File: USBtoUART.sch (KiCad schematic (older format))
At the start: 17 parts

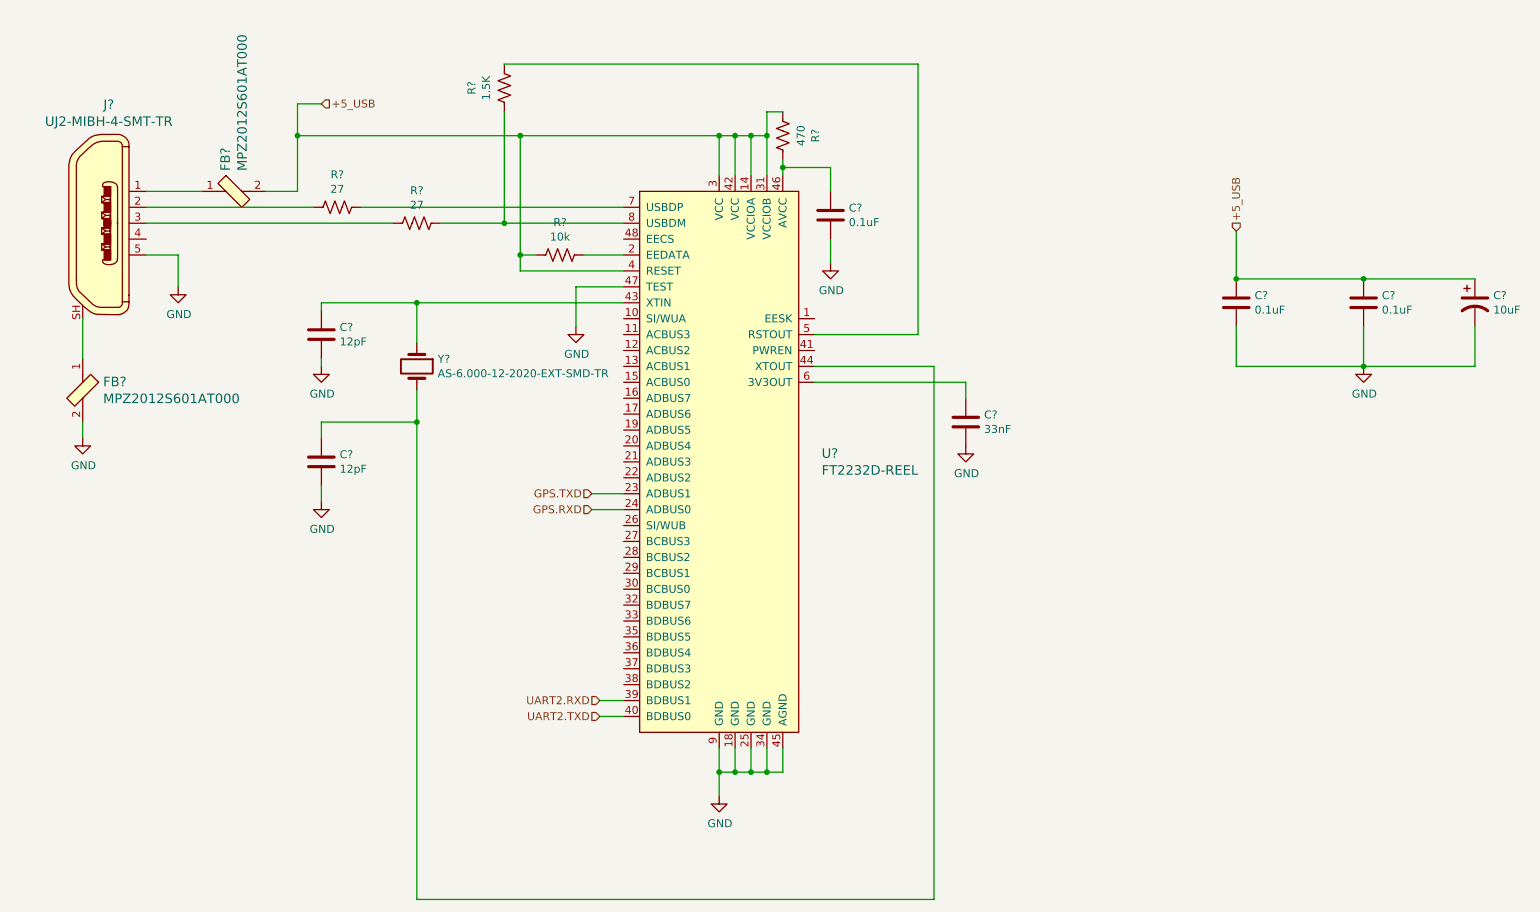
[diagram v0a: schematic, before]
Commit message: Annotated schematics and added UART Jumpers
Annotated schematics.

Added jumpers to GPS UART because I'm still not 100% sure on the connections and I don't want to have to respin a board because I was wrong.
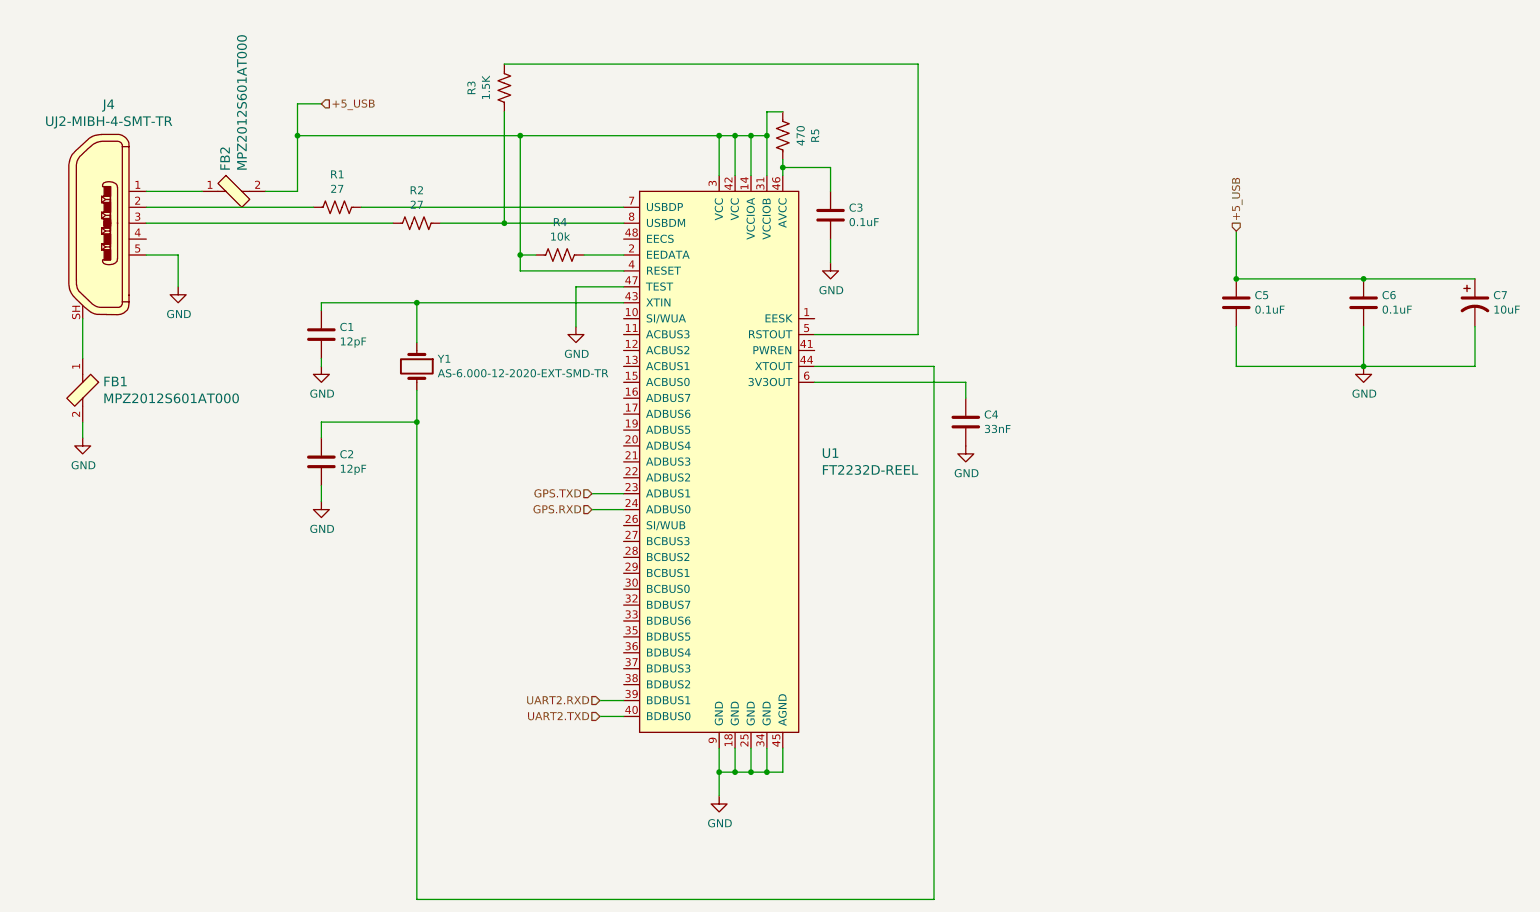
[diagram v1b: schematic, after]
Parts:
- gave numbers to parts that had none: 17
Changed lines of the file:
@@
 $EndDescr
 $Comp
-L dk_Interface-Controllers:FT2232D-REEL U?
+L dk_Interface-Controllers:FT2232D-REEL U1
 U 1 1 5F8465F0
 P 5450 2500
-F 0 "U?" H 5894 1453 60  0000 L CNN
+F 0 "U1" H 5894 1453 60  0000 L CNN
 F 1 "FT2232D-REEL" H 5894 1347 60  0000 L CNN
 F 2 "digikey-footprints:LQFP-48_7x7mm" V 5650 2700 60  0001 L CNN
@@
 $EndComp
 $Comp
-L dk_USB-DVI-HDMI-Connectors:UJ2-MIBH-4-SMT-TR J?
+L dk_USB-DVI-HDMI-Connectors:UJ2-MIBH-4-SMT-TR J4
 U 1 1 5F847751
 P 1350 2100
-F 0 "J?" H 1414 2845 60  0000 C CNN
+F 0 "J4" H 1414 2845 60  0000 C CNN
 F 1 "UJ2-MIBH-4-SMT-TR" H 1414 2739 60  0000 C CNN
 F 2 "digikey-footprints:USB_Micro_B_Male_UJ2-MIBH-4-SMT-TR" H 1550 2300 60  0001 L CNN
@@
 $EndComp
 $Comp
-L power:GND #PWR?
+L power:GND #PWR03
 U 1 1 5F848CF8
 P 1850 2500
-F 0 "#PWR?" H 1850 2250 50  0001 C CNN
+F 0 "#PWR03" H 1850 2250 50  0001 C CNN
 F 1 "GND" H 1855 2327 50  0000 C CNN
 F 2 "" H 1850 2500 50  0001 C CNN
@@
 $EndComp
 $Comp
-L dk_Ferrite-Beads-and-Chips:MPZ2012S601AT000 FB?
+L dk_Ferrite-Beads-and-Chips:MPZ2012S601AT000 FB1
 U 1 1 5F84934E
 P 1250 3150
-F 0 "FB?" V 1197 3278 60  0000 L CNN
+F 0 "FB1" V 1197 3278 60  0000 L CNN
 F 1 "MPZ2012S601AT000" V 1303 3278 60  0000 L CNN
 F 2 "digikey-footprints:0805" H 1450 3350 60  0001 L CNN
@@
 	1250 2700 1250 2950
 $Comp
-L power:GND #PWR?
+L power:GND #PWR02
 U 1 1 5F84BCF3
 P 1250 3450
-F 0 "#PWR?" H 1250 3200 50  0001 C CNN
+F 0 "#PWR02" H 1250 3200 50  0001 C CNN
 F 1 "GND" H 1255 3277 50  0000 C CNN
 F 2 "" H 1250 3450 50  0001 C CNN
@@
 	1250 3350 1250 3450
 $Comp
-L dk_Ferrite-Beads-and-Chips:MPZ2012S601AT000 FB?
+L dk_Ferrite-Beads-and-Chips:MPZ2012S601AT000 FB2
 U 1 1 5F84C701
 P 2200 1900
-F 0 "FB?" V 2147 2028 60  0000 L CNN
+F 0 "FB2" V 2147 2028 60  0000 L CNN
 F 1 "MPZ2012S601AT000" V 2253 2028 60  0000 L CNN
 F 2 "digikey-footprints:0805" H 2400 2100 60  0001 L CNN
@@
 	1650 1900 2000 1900
 $Comp
-L Device:C C?
+L Device:C C4
 U 1 1 5F84E28B
 P 6800 3350
-F 0 "C?" H 6915 3396 50  0000 L CNN
+F 0 "C4" H 6915 3396 50  0000 L CNN
 F 1 "33nF" H 6915 3305 50  0000 L CNN
 F 2 "Capacitor_SMD:C_0805_2012Metric_Pad1.18x1.45mm_HandSolder" H 6800 3350 50  0001 C CNN
@@
 	6800 3100 6800 3200
 $Comp
-L Device:C C?
+L Device:C C5
 U 1 1 5F84FF63
 P 8500 2600
-F 0 "C?" H 8615 2646 50  0000 L CNN
+F 0 "C5" H 8615 2646 50  0000 L CNN
 F 1 "0.1uF" H 8615 2555 50  0000 L CNN
 F 2 "Capacitor_SMD:C_0805_2012Metric_Pad1.18x1.45mm_HandSolder" H 8500 2600 50  0001 C CNN
@@
 $EndComp
 $Comp
-L Device:C C?
+L Device:C C6
 U 1 1 5F850987
 P 9300 2600
-F 0 "C?" H 9415 2646 50  0000 L CNN
+F 0 "C6" H 9415 2646 50  0000 L CNN
 F 1 "0.1uF" H 9415 2555 50  0000 L CNN
 F 2 "Capacitor_SMD:C_0805_2012Metric_Pad1.18x1.45mm_HandSolder" H 9300 2600 50  0001 C CNN
@@
 $EndComp
 $Comp
-L Device:CP1 C?
+L Device:CP1 C7
 U 1 1 5F853226
 P 10000 2600
-F 0 "C?" H 10115 2646 50  0000 L CNN
+F 0 "C7" H 10115 2646 50  0000 L CNN
 F 1 "10uF" H 10115 2555 50  0000 L CNN
 F 2 "Capacitor_Tantalum_SMD:CP_EIA-3216-10_Kemet-I_Pad1.58x1.35mm_HandSolder" H 10000 2600 50  0001 C CNN
@@
 $EndComp
 $Comp
-L Device:R_US R?
+L Device:R_US R1
 U 1 1 5F85B62B
 P 2850 2000
-F 0 "R?" V 2645 2000 50  0000 C CNN
+F 0 "R1" V 2645 2000 50  0000 C CNN
 F 1 "27" V 2736 2000 50  0000 C CNN
 F 2 "Resistor_SMD:R_0805_2012Metric_Pad1.20x1.40mm_HandSolder" V 2890 1990 50  0001 C CNN
@@
 $EndComp
 $Comp
-L Device:R_US R?
+L Device:R_US R2
 U 1 1 5F85C9ED
 P 3350 2100
-F 0 "R?" V 3145 2100 50  0000 C CNN
+F 0 "R2" V 3145 2100 50  0000 C CNN
 F 1 "27" V 3236 2100 50  0000 C CNN
 F 2 "Resistor_SMD:R_0805_2012Metric_Pad1.20x1.40mm_HandSolder" V 3390 2090 50  0001 C CNN
@@
 	1650 2100 3200 2100
 $Comp
-L Device:R_US R?
+L Device:R_US R3
 U 1 1 5F85D849
 P 3900 1250
-F 0 "R?" V 3695 1250 50  0000 C CNN
+F 0 "R3" V 3695 1250 50  0000 C CNN
 F 1 "1.5K" V 3786 1250 50  0000 C CNN
 F 2 "Resistor_SMD:R_0805_2012Metric_Pad1.20x1.40mm_HandSolder" V 3940 1240 50  0001 C CNN
@@
 	4500 5100 4650 5100
 $Comp
-L Device:Crystal Y?
+L Device:Crystal Y1
 U 1 1 5F86847C
 P 3350 3000
-F 0 "Y?" V 3304 3131 50  0000 L CNN
+F 0 "Y1" V 3304 3131 50  0000 L CNN
 F 1 "AS-6.000-12-2020-EXT-SMD-TR" V 3395 3131 50  0000 L CNN
 F 2 "Crystal:Crystal_SMD_HC49-SD_HandSoldering" H 3350 3000 50  0001 C CNN
@@
 	6600 3000 5850 3000
 $Comp
-L Device:C C?
+L Device:C C1
 U 1 1 5F869A1D
 P 2750 2800
-F 0 "C?" H 2865 2846 50  0000 L CNN
+F 0 "C1" H 2865 2846 50  0000 L CNN
 F 1 "12pF" H 2865 2755 50  0000 L CNN
 F 2 "Capacitor_SMD:C_0805_2012Metric_Pad1.18x1.45mm_HandSolder" H 2750 2800 50  0001 C CNN
@@
 $EndComp
 $Comp
-L Device:C C?
+L Device:C C2
 U 1 1 5F86A608
 P 2750 3600
-F 0 "C?" H 2865 3646 50  0000 L CNN
+F 0 "C2" H 2865 3646 50  0000 L CNN
 F 1 "12pF" H 2865 3555 50  0000 L CNN
 F 2 "Capacitor_SMD:C_0805_2012Metric_Pad1.18x1.45mm_HandSolder" H 2750 3600 50  0001 C CNN
@@
 $EndComp
 $Comp
-L power:GND #PWR?
+L power:GND #PWR04
 U 1 1 5F86A976
 P 2750 3000
-F 0 "#PWR?" H 2750 2750 50  0001 C CNN
+F 0 "#PWR04" H 2750 2750 50  0001 C CNN
 F 1 "GND" H 2755 2827 50  0000 C CNN
 F 2 "" H 2750 3000 50  0001 C CNN
@@
 $EndComp
 $Comp
-L power:GND #PWR?
+L power:GND #PWR05
 U 1 1 5F86AC39
 P 2750 3850
-F 0 "#PWR?" H 2750 3600 50  0001 C CNN
+F 0 "#PWR05" H 2750 3600 50  0001 C CNN
 F 1 "GND" H 2755 3677 50  0000 C CNN
 F 2 "" H 2750 3850 50  0001 C CNN
@@
 	2750 2950 2750 3000
 $Comp
-L power:GND #PWR?
+L power:GND #PWR010
 U 1 1 5F88F94A
 P 9300 3000
-F 0 "#PWR?" H 9300 2750 50  0001 C CNN
+F 0 "#PWR010" H 9300 2750 50  0001 C CNN
 F 1 "GND" H 9305 2827 50  0000 C CNN
 F 2 "" H 9300 3000 50  0001 C CNN
@@
 	5250 1550 5350 1550
 $Comp
-L Device:C C?
+L Device:C C3
 U 1 1 5F894C10
 P 5950 2050
-F 0 "C?" H 6065 2096 50  0000 L CNN
+F 0 "C3" H 6065 2096 50  0000 L CNN
 F 1 "0.1uF" H 6065 2005 50  0000 L CNN
 F 2 "Capacitor_SMD:C_0805_2012Metric_Pad1.18x1.45mm_HandSolder" H 5950 2050 50  0001 C CNN
@@
 $EndComp
 $Comp
-L Device:R_US R?
+L Device:R_US R5
 U 1 1 5F895D20
 P 5650 1550
-F 0 "R?" V 5445 1550 50  0000 C CNN
+F 0 "R5" V 5445 1550 50  0000 C CNN
 F 1 "470" V 5536 1550 50  0000 C CNN
 F 2 "Resistor_SMD:R_0805_2012Metric_Pad1.20x1.40mm_HandSolder" V 5690 1540 50  0001 C CNN
@@
 Connection ~ 5550 1550
 $Comp
-L power:GND #PWR?
+L power:GND #PWR08
 U 1 1 5F898B74
 P 5950 2350
-F 0 "#PWR?" H 5950 2100 50  0001 C CNN
+F 0 "#PWR08" H 5950 2100 50  0001 C CNN
 F 1 "GND" H 5955 2177 50  0000 C CNN
 F 2 "" H 5950 2350 50  0001 C CNN
@@
 	5950 2350 5950 2200
 $Comp
-L power:GND #PWR?
+L power:GND #PWR09
 U 1 1 5F899BAF
 P 6800 3500
-F 0 "#PWR?" H 6800 3250 50  0001 C CNN
+F 0 "#PWR09" H 6800 3250 50  0001 C CNN
 F 1 "GND" H 6805 3327 50  0000 C CNN
 F 2 "" H 6800 3500 50  0001 C CNN
@@
 Connection ~ 9300 2450
 $Comp
-L power:GND #PWR?
+L power:GND #PWR07
 U 1 1 5F89EA9A
 P 5250 5700
-F 0 "#PWR?" H 5250 5450 50  0001 C CNN
+F 0 "#PWR07" H 5250 5450 50  0001 C CNN
 F 1 "GND" H 5255 5527 50  0000 C CNN
 F 2 "" H 5250 5700 50  0001 C CNN
@@
 	5550 5550 5450 5550
 $Comp
-L power:GND #PWR?
+L power:GND #PWR06
 U 1 1 5F8A43C4
 P 4350 2750
-F 0 "#PWR?" H 4350 2500 50  0001 C CNN
+F 0 "#PWR06" H 4350 2500 50  0001 C CNN
 F 1 "GND" H 4355 2577 50  0000 C CNN
 F 2 "" H 4350 2750 50  0001 C CNN
@@
 	5850 2800 6500 2800
 $Comp
-L Device:R_US R?
+L Device:R_US R4
 U 1 1 5F8B2661
 P 4250 2300
-F 0 "R?" V 4045 2300 50  0000 C CNN
+F 0 "R4" V 4045 2300 50  0000 C CNN
 F 1 "10k" V 4136 2300 50  0000 C CNN
 F 2 "Resistor_SMD:R_0805_2012Metric_Pad1.20x1.40mm_HandSolder" V 4290 2290 50  0001 C CNN

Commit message: completed connections
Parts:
- added JP? (x2): JUMPER-SMT_3_1-NC, SMT-JUMPER_3_1-NC, symbol SparkFun-Jumpers:JUMPER-SMT_3_1-NC
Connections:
- net UART2.RXD: now also JP?.1, JP?.3; no longer U1.39 (BDBUS1)
- net UART2.TXD: now also JP?.1, JP?.3; no longer U1.40 (BDBUS0)
- new net: JP?.2, U1.39 (BDBUS1)
- new net: JP?.2, U1.40 (BDBUS0)
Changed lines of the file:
@@
 $Descr A4 11693 8268
 encoding utf-8
-Sheet 3 4
+Sheet 2 4
 Title ""
 Date ""
@@
 Wire Wire Line
 	4450 3800 4650 3800
-Text HLabel 4500 5100 0    50   Input ~ 0
+Text HLabel 1400 4800 0    50   Input ~ 0
 UART2.RXD
-Text HLabel 4500 5200 0    50   Input ~ 0
+Text HLabel 1400 5900 0    50   Input ~ 0
 UART2.TXD
-Wire Wire Line
-	4500 5200 4650 5200
-Wire Wire Line
-	4500 5100 4650 5100
 $Comp
 L Device:Crystal Y1
@@
 Wire Wire Line
 	4400 2300 4650 2300
+$Comp
+L SparkFun-Jumpers:JUMPER-SMT_3_1-NC JP?
+U 1 1 5F8D37AA
+P 2000 5000
+F 0 "JP?" H 2104 4905 45  0000 L CNN
+F 1 "JUMPER-SMT_3_1-NC" H 2104 4989 45  0000 L CNN
+F 2 "SMT-JUMPER_3_1-NC" H 2000 5250 20  0001 C CNN
+F 3 "" V 2000 4945 60  0001 C CNN
+F 4 "XXX-00000" H 2104 5084 60  0000 L CNN "PROD_ID"
+	1    2000 5000
+	-1   0    0    1
+$EndComp
+$Comp
+L SparkFun-Jumpers:JUMPER-SMT_3_1-NC JP?
+U 1 1 5F8DF40E
+P 1750 5700
+F 0 "JP?" H 1854 5605 45  0000 L CNN
+F 1 "JUMPER-SMT_3_1-NC" H 1854 5689 45  0000 L CNN
+F 2 "SMT-JUMPER_3_1-NC" H 1750 5950 20  0001 C CNN
+F 3 "" V 1750 5645 60  0001 C CNN
+F 4 "XXX-00000" H 1854 5784 60  0000 L CNN "PROD_ID"
+	1    1750 5700
+	-1   0    0    -1
+$EndComp
+Wire Wire Line
+	1900 5700 4150 5700
+Wire Wire Line
+	4150 5700 4150 5200
+Wire Wire Line
+	4150 5200 4650 5200
+Wire Wire Line
+	2150 5000 4350 5000
+Wire Wire Line
+	4350 5000 4350 5100
+Wire Wire Line
+	4350 5100 4650 5100
+Wire Wire Line
+	1400 5900 1750 5900
+Wire Wire Line
+	1750 5900 2000 5900
+Wire Wire Line
+	2000 5900 2000 5200
+Connection ~ 1750 5900
+Wire Wire Line
+	2000 4800 1750 4800
+Wire Wire Line
+	1750 5500 1750 4800
+Connection ~ 1750 4800
+Wire Wire Line
+	1750 4800 1400 4800
 $EndSCHEMATC
